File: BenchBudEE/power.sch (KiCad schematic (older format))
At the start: 11 parts

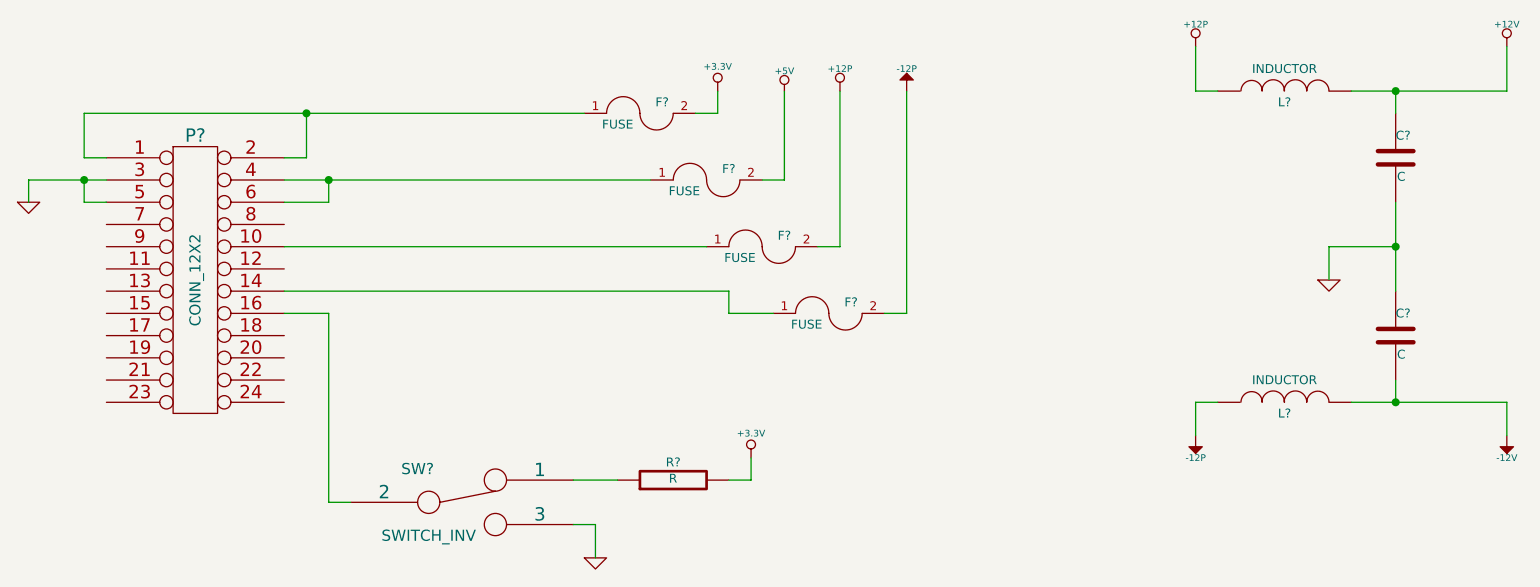
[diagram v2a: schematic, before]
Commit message: fan/current supply refactor
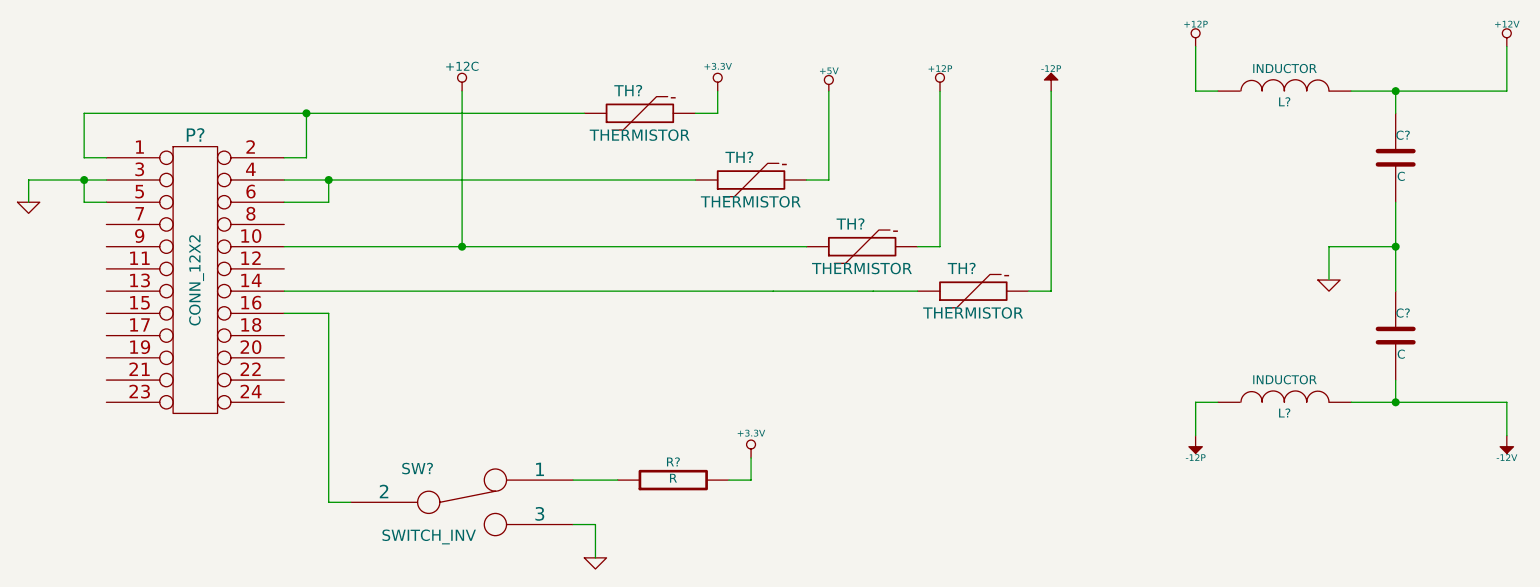
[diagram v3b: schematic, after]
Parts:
- removed F? (x4): FUSE, ~, symbol FUSE
- added TH? (x4): THERMISTOR, ~, symbol THERMISTOR
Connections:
- net +12P: now also TH?.2
- net +3.3V: now also TH?.2
- net +5V: now also TH?.2
- net -12P: now also TH?.2
- net at P?.1 (P1), P?.2 (P2): now also TH?.1
- net +12C: now reaches P?.10 (P10)
- net +12C: now also TH?.1
- net at P?.14 (P14): now also TH?.1
- net at P?.4 (P4), P?.6 (P6): now also TH?.1
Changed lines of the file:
@@
 L +5V #PWR?
 U 1 1 52FADD4C
-P 6550 2300
-F 0 "#PWR?" H 6550 2390 20  0001 C CNN
-F 1 "+5V" H 6550 2390 30  0000 C CNN
-F 2 "" H 6550 2300 60  0000 C CNN
-F 3 "" H 6550 2300 60  0000 C CNN
-	1    6550 2300
+P 6750 2300
+F 0 "#PWR?" H 6750 2390 20  0001 C CNN
+F 1 "+5V" H 6750 2390 30  0000 C CNN
+F 2 "" H 6750 2300 60  0000 C CNN
+F 3 "" H 6750 2300 60  0000 C CNN
+	1    6750 2300
 	1    0    0    -1
 $EndComp
@@
 $EndComp
 $Comp
-L FUSE F?
-U 1 1 52FADD7E
-P 6200 2700
-F 0 "F?" H 6300 2750 40  0000 C CNN
-F 1 "FUSE" H 6100 2650 40  0000 C CNN
-F 2 "~" H 6200 2700 60  0000 C CNN
-F 3 "~" H 6200 2700 60  0000 C CNN
-	1    6200 2700
-	1    0    0    -1
-$EndComp
-$Comp
-L FUSE F?
-U 1 1 52FADD95
-P 5900 2400
-F 0 "F?" H 6000 2450 40  0000 C CNN
-F 1 "FUSE" H 5800 2350 40  0000 C CNN
-F 2 "~" H 5900 2400 60  0000 C CNN
-F 3 "~" H 5900 2400 60  0000 C CNN
-	1    5900 2400
-	1    0    0    -1
-$EndComp
-$Comp
-L FUSE F?
-U 1 1 52FADD9B
-P 6450 3000
-F 0 "F?" H 6550 3050 40  0000 C CNN
-F 1 "FUSE" H 6350 2950 40  0000 C CNN
-F 2 "~" H 6450 3000 60  0000 C CNN
-F 3 "~" H 6450 3000 60  0000 C CNN
-	1    6450 3000
-	1    0    0    -1
-$EndComp
-$Comp
-L FUSE F?
-U 1 1 52FADDA1
-P 6750 3300
-F 0 "F?" H 6850 3350 40  0000 C CNN
-F 1 "FUSE" H 6650 3250 40  0000 C CNN
-F 2 "~" H 6750 3300 60  0000 C CNN
-F 3 "~" H 6750 3300 60  0000 C CNN
-	1    6750 3300
-	1    0    0    -1
-$EndComp
-$Comp
 L SWITCH_INV SW?
 U 1 1 52FADDA9
@@
 L +12P #PWR?
 U 1 1 52FADE58
-P 6800 2300
-F 0 "#PWR?" H 6800 2270 30  0001 C CNN
-F 1 "+12P" H 6800 2400 30  0000 C CNN
-F 2 "" H 6800 2300 60  0000 C CNN
-F 3 "" H 6800 2300 60  0000 C CNN
-	1    6800 2300
+P 7250 2300
+F 0 "#PWR?" H 7250 2270 30  0001 C CNN
+F 1 "+12P" H 7250 2400 30  0000 C CNN
+F 2 "" H 7250 2300 60  0000 C CNN
+F 3 "" H 7250 2300 60  0000 C CNN
+	1    7250 2300
 	1    0    0    -1
 $EndComp
@@
 L -12P #PWR?
 U 1 1 52FADECA
-P 7100 2300
-F 0 "#PWR?" H 7100 2430 20  0001 C CNN
-F 1 "-12P" H 7100 2400 30  0000 C CNN
-F 2 "" H 7100 2300 60  0000 C CNN
-F 3 "" H 7100 2300 60  0000 C CNN
-	1    7100 2300
+P 7750 2300
+F 0 "#PWR?" H 7750 2430 20  0001 C CNN
+F 1 "-12P" H 7750 2400 30  0000 C CNN
+F 2 "" H 7750 2300 60  0000 C CNN
+F 3 "" H 7750 2300 60  0000 C CNN
+	1    7750 2300
 	1    0    0    -1
 $EndComp
@@
 $EndComp
 Wire Wire Line
-	9100 3700 9800 3700
+	9100 3700 9300 3700
+Wire Wire Line
+	9300 3700 9800 3700
 Wire Wire Line
 	9300 3600 9300 3700
 Connection ~ 9300 3000
 Wire Wire Line
-	9300 2800 9300 3200
+	9300 2800 9300 3000
+Wire Wire Line
+	9300 3000 9300 3200
 Wire Wire Line
 	9000 3000 9300 3000
@@
 	3400 2800 3500 2800
 Wire Wire Line
-	7100 3300 7000 3300
-Wire Wire Line
-	7100 2300 7100 3300
-Wire Wire Line
-	6300 3300 6500 3300
-Wire Wire Line
-	6300 3200 6300 3300
-Wire Wire Line
-	4300 3200 6300 3200
-Wire Wire Line
-	6800 3000 6700 3000
-Wire Wire Line
-	6800 2300 6800 3000
-Wire Wire Line
-	4300 3000 6200 3000
+	7750 3200 7650 3200
+Wire Wire Line
+	7750 2300 7750 3200
+Wire Wire Line
+	6950 3200 7150 3200
+Wire Wire Line
+	6500 3200 6950 3200
+Wire Wire Line
+	4300 3200 6500 3200
+Wire Wire Line
+	7250 3000 7150 3000
+Wire Wire Line
+	7250 2300 7250 3000
+Wire Wire Line
+	4300 3000 5100 3000
+Wire Wire Line
+	5100 3000 6650 3000
 Wire Wire Line
 	6250 2400 6250 2300
@@
 	4300 2600 4400 2600
 Wire Wire Line
-	3400 2400 5650 2400
+	3400 2400 4400 2400
+Wire Wire Line
+	4400 2400 5650 2400
 Wire Wire Line
 	3400 2600 3400 2400
@@
 	4300 2800 4500 2800
 Wire Wire Line
-	4300 2700 5950 2700
-Wire Wire Line
-	6550 2700 6550 2300
-Wire Wire Line
-	6450 2700 6550 2700
+	4300 2700 4500 2700
+Wire Wire Line
+	4500 2700 6150 2700
+Wire Wire Line
+	6750 2700 6750 2300
+Wire Wire Line
+	6650 2700 6750 2700
 Wire Wire Line
 	3150 2700 3150 2800
 Wire Wire Line
-	3150 2700 3500 2700
+	3150 2700 3400 2700
+Wire Wire Line
+	3400 2700 3500 2700
 Wire Wire Line
 	8500 3700 8400 3700
@@
 	9300 2400 9300 2300
 Wire Wire Line
-	9100 2300 9800 2300
+	9100 2300 9300 2300
+Wire Wire Line
+	9300 2300 9800 2300
 Wire Wire Line
 	8500 2300 8400 2300
@@
 	9800 2300 9800 2100
 Connection ~ 9300 2300
+Wire Wire Line
+	5100 3000 5100 2300
+Connection ~ 5100 3000
+$Comp
+L +12C #PWR?
+U 1 1 5302A69A
+P 5100 2300
+F 0 "#PWR?" H 5100 2270 30  0001 C CNN
+F 1 "+12C" H 5100 2410 40  0000 C CNN
+F 2 "" H 5100 2300 60  0000 C CNN
+F 3 "" H 5100 2300 60  0000 C CNN
+	1    5100 2300
+	1    0    0    -1
+$EndComp
+$Comp
+L THERMISTOR TH?
+U 1 1 5302A964
+P 5900 2400
+F 0 "TH?" V 6000 2450 50  0000 C CNN
+F 1 "THERMISTOR" V 5800 2400 50  0000 C CNN
+F 2 "~" H 5900 2400 60  0000 C CNN
+F 3 "~" H 5900 2400 60  0000 C CNN
+	1    5900 2400
+	0    -1   -1   0
+$EndComp
+$Comp
+L THERMISTOR TH?
+U 1 1 5302A980
+P 6400 2700
+F 0 "TH?" V 6500 2750 50  0000 C CNN
+F 1 "THERMISTOR" V 6300 2700 50  0000 C CNN
+F 2 "~" H 6400 2700 60  0000 C CNN
+F 3 "~" H 6400 2700 60  0000 C CNN
+	1    6400 2700
+	0    -1   -1   0
+$EndComp
+$Comp
+L THERMISTOR TH?
+U 1 1 5302A986
+P 6900 3000
+F 0 "TH?" V 7000 3050 50  0000 C CNN
+F 1 "THERMISTOR" V 6800 3000 50  0000 C CNN
+F 2 "~" H 6900 3000 60  0000 C CNN
+F 3 "~" H 6900 3000 60  0000 C CNN
+	1    6900 3000
+	0    -1   -1   0
+$EndComp
+$Comp
+L THERMISTOR TH?
+U 1 1 5302A98C
+P 7400 3200
+F 0 "TH?" V 7500 3250 50  0000 C CNN
+F 1 "THERMISTOR" V 7300 3200 50  0000 C CNN
+F 2 "~" H 7400 3200 60  0000 C CNN
+F 3 "~" H 7400 3200 60  0000 C CNN
+	1    7400 3200
+	0    -1   -1   0
+$EndComp
 $EndSCHEMATC
